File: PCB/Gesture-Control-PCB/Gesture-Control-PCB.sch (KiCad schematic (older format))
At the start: 5 parts, among them J1 Jack-DC, J2 Conn_01x07_Female, U1 L7806CV, U2 LD1117V33, U3 NodeMCU1.0(ESP-12E)

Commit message: decrease size, fit all components under nodemcu
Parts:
- U1, U2: footprint Package_TO_SOT_THT:TO-220-3_Vertical -> Package_TO_SOT_THT:TO-220-3_Horizontal_TabDown
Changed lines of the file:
@@
 F 0 "U2" H 3050 4092 50  0000 C CNN
 F 1 "LD1117V33" H 3050 4001 50  0000 C CNN
-F 2 "Package_TO_SOT_THT:TO-220-3_Vertical" H 3075 3700 50  0001 L CIN
+F 2 "Package_TO_SOT_THT:TO-220-3_Horizontal_TabDown" H 3075 3700 50  0001 L CIN
 F 3 "http://www.st.com/content/ccc/resource/technical/document/datasheet/41/4f/b3/b0/12/d4/47/88/CD00000444.pdf/files/CD00000444.pdf/jcr:content/translations/en.CD00000444.pdf" H 3050 3800 50  0001 C CNN
 	1    3050 3850
@@
 F 0 "U1" H 3050 3242 50  0000 C CNN
 F 1 "L7806CV" H 3050 3151 50  0000 C CNN
-F 2 "Package_TO_SOT_THT:TO-220-3_Vertical" H 3075 2850 50  0001 L CIN
+F 2 "Package_TO_SOT_THT:TO-220-3_Horizontal_TabDown" H 3075 2850 50  0001 L CIN
 F 3 "http://www.st.com/content/ccc/resource/technical/document/datasheet/41/4f/b3/b0/12/d4/47/88/CD00000444.pdf/files/CD00000444.pdf/jcr:content/translations/en.CD00000444.pdf" H 3050 2950 50  0001 C CNN
 	1    3050 3000

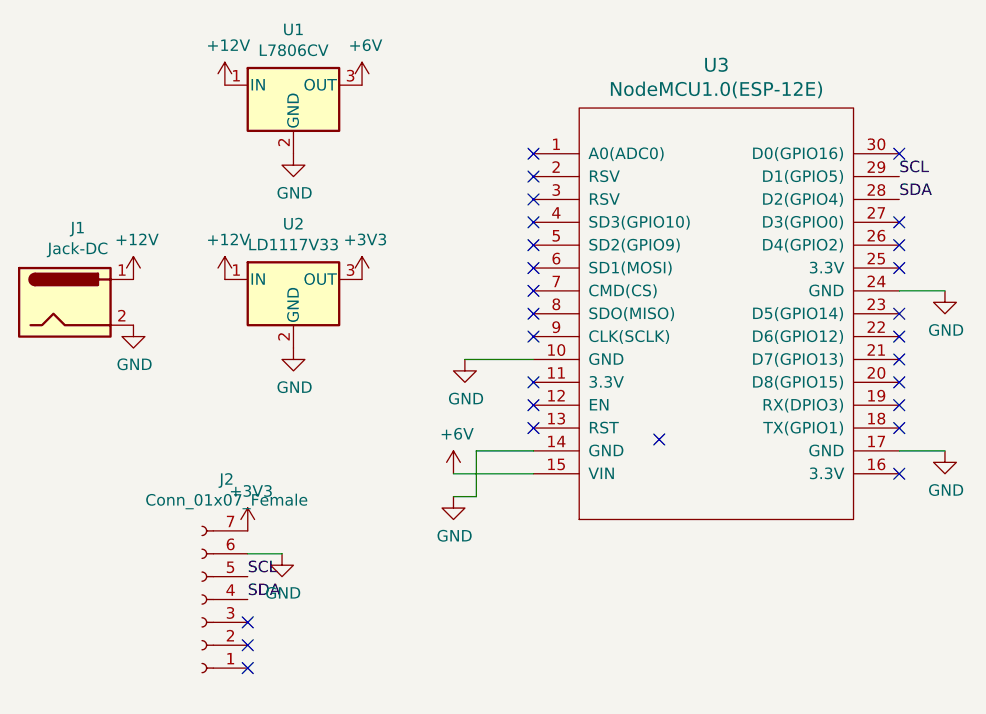
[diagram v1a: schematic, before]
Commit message: removed one voltage regulator (lmao im a dummy)
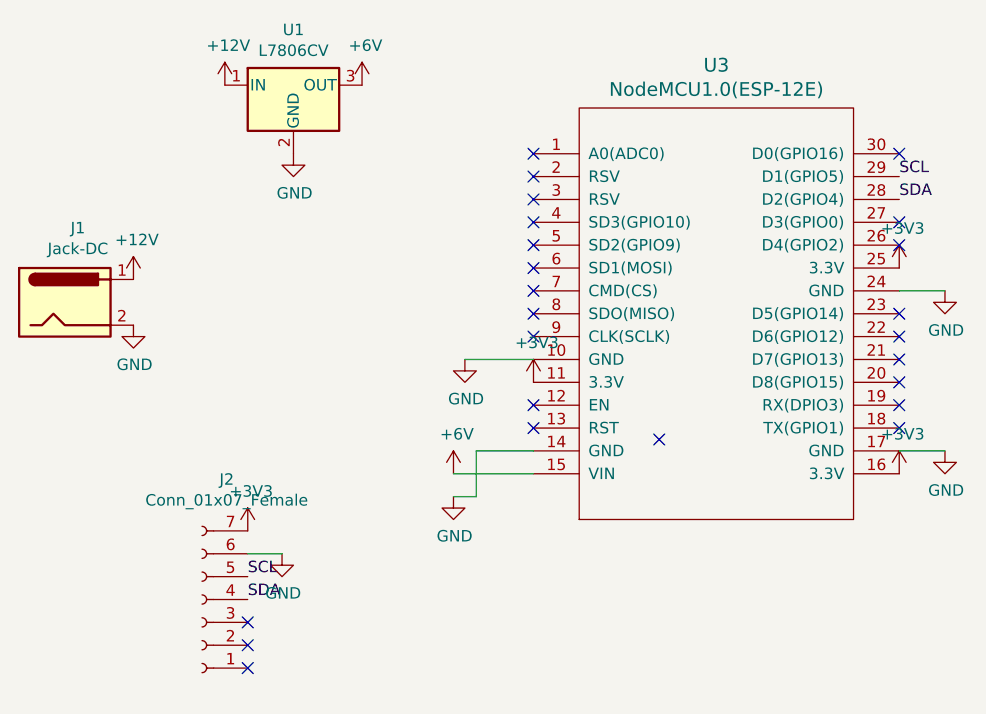
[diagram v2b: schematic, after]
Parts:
- removed U2: LD1117V33, Package_TO_SOT_THT:TO-220-3_Horizontal_TabDown, symbol Regulator_Linear:L7805
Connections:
- net +3V3: now also U3.11 (3.3V), U3.16 (3.3V), U3.25 (3.3V)
- no-connect marks 27 -> 24
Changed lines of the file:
@@
-$EndComp
-$Comp
-L Regulator_Linear:L7805 U2
-U 1 1 5FB5574C
-P 3050 3850
-F 0 "U2" H 3050 4092 50  0000 C CNN
-F 1 "LD1117V33" H 3050 4001 50  0000 C CNN
-F 2 "Package_TO_SOT_THT:TO-220-3_Horizontal_TabDown" H 3075 3700 50  0001 L CIN
-F 3 "http://www.st.com/content/ccc/resource/technical/document/datasheet/41/4f/b3/b0/12/d4/47/88/CD00000444.pdf/files/CD00000444.pdf/jcr:content/translations/en.CD00000444.pdf" H 3050 3800 50  0001 C CNN
-	1    3050 3850
-	1    0    0    -1
-$EndComp
-$Comp
-L power:+12V #PWR04
-U 1 1 5FB56752
-P 2750 3850
-F 0 "#PWR04" H 2750 3700 50  0001 C CNN
-F 1 "+12V" H 2765 4023 50  0000 C CNN
-F 2 "" H 2750 3850 50  0001 C CNN
-F 3 "" H 2750 3850 50  0001 C CNN
-	1    2750 3850
-	1    0    0    -1
-$EndComp
-$Comp
-L power:GND #PWR08
-U 1 1 5FB56B3F
-P 3050 4150
-F 0 "#PWR08" H 3050 3900 50  0001 C CNN
-F 1 "GND" H 3055 3977 50  0000 C CNN
-F 2 "" H 3050 4150 50  0001 C CNN
-F 3 "" H 3050 4150 50  0001 C CNN
-	1    3050 4150
-	1    0    0    -1
-$EndComp
-$Comp
-L power:+3V3 #PWR010
-U 1 1 5FB57184
-P 3350 3850
-F 0 "#PWR010" H 3350 3700 50  0001 C CNN
-F 1 "+3V3" H 3365 4023 50  0000 C CNN
-F 2 "" H 3350 3850 50  0001 C CNN
-F 3 "" H 3350 3850 50  0001 C CNN
-	1    3350 3850
-	1    0    0    -1
 $EndComp
 $Comp
@@
 NoConn ~ 4100 4000
 NoConn ~ 4100 4100
-NoConn ~ 4100 4300
 NoConn ~ 4100 4400
 NoConn ~ 4100 4500
-NoConn ~ 5700 4700
 NoConn ~ 5700 4500
 NoConn ~ 5700 4400
@@
 NoConn ~ 5700 4100
 NoConn ~ 5700 4000
-NoConn ~ 5700 3800
 NoConn ~ 5700 3700
 NoConn ~ 5700 3600
@@
 NoConn ~ 5700 3300
 NoConn ~ 4650 4550
+$Comp
+L power:+3V3 #PWR08
+U 1 1 5FB5C1C7
+P 5700 3800
+F 0 "#PWR08" H 5700 3650 50  0001 C CNN
+F 1 "+3V3" H 5715 3973 50  0000 C CNN
+F 2 "" H 5700 3800 50  0001 C CNN
+F 3 "" H 5700 3800 50  0001 C CNN
+	1    5700 3800
+	1    0    0    -1
+$EndComp
+$Comp
+L power:+3V3 #PWR010
+U 1 1 5FB5E0A4
+P 5700 4700
+F 0 "#PWR010" H 5700 4550 50  0001 C CNN
+F 1 "+3V3" H 5715 4873 50  0000 C CNN
+F 2 "" H 5700 4700 50  0001 C CNN
+F 3 "" H 5700 4700 50  0001 C CNN
+	1    5700 4700
+	1    0    0    -1
+$EndComp
+$Comp
+L power:+3V3 #PWR04
+U 1 1 5FB5EB1B
+P 4100 4300
+F 0 "#PWR04" H 4100 4150 50  0001 C CNN
+F 1 "+3V3" H 4115 4473 50  0000 C CNN
+F 2 "" H 4100 4300 50  0001 C CNN
+F 3 "" H 4100 4300 50  0001 C CNN
+	1    4100 4300
+	1    0    0    -1
+$EndComp
 $EndSCHEMATC

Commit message: fixed mpu socket and moved shit to bottom layer
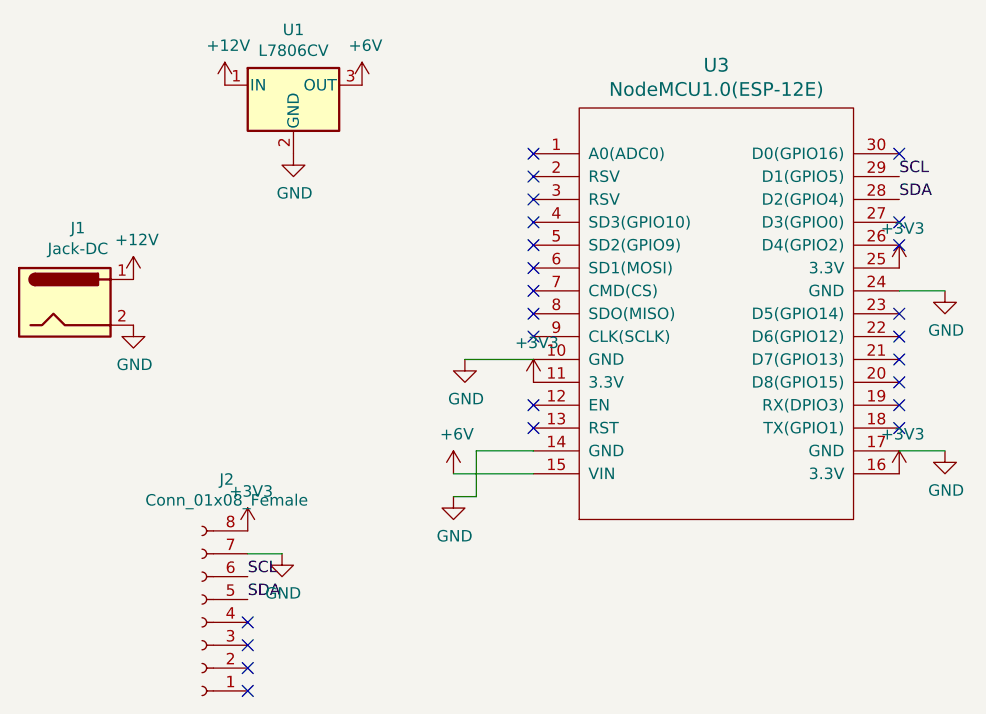
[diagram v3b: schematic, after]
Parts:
- removed J2: Conn_01x07_Female, Connector_PinSocket_2.00mm:PinSocket_1x07_P2.00mm_Vertical, symbol Connector:Conn_01x07_Female
- added J2: Conn_01x08_Female, Connector_PinSocket_2.54mm:PinSocket_1x08_P2.54mm_Vertical, symbol Connector:Conn_01x08_Female
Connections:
- net +3V3: now also J2.8 (Pin_8)
- net GND: now also J2.7 (Pin_7)
- net SCL: now also J2.6 (Pin_6)
- net SDA: now also J2.5 (Pin_5)
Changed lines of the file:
@@
 Text Label 2850 5150 0    50   ~ 0
 SCL
-$Comp
-L Connector:Conn_01x07_Female J2
-U 1 1 5FB66EDE
-P 2650 5250
-F 0 "J2" H 2542 4725 50  0000 C CNN
-F 1 "Conn_01x07_Female" H 2542 4816 50  0000 C CNN
-F 2 "Connector_PinSocket_2.00mm:PinSocket_1x07_P2.00mm_Vertical" H 2650 5250 50  0001 C CNN
-F 3 "~" H 2650 5250 50  0001 C CNN
-	1    2650 5250
-	-1   0    0    1
-$EndComp
 Text Label 5700 3400 0    50   ~ 0
 SCL
@@
 Text Label 5700 3500 0    50   ~ 0
 SDA
-NoConn ~ 2850 5350
-NoConn ~ 2850 5450
-NoConn ~ 2850 5550
 NoConn ~ 4100 3300
 NoConn ~ 4100 3400
@@
 	3800 4200 4100 4200
 NoConn ~ 5700 3300
-NoConn ~ 4650 4550
 $Comp
 L power:+3V3 #PWR08
@@
 	1    0    0    -1
 $EndComp
+$Comp
+L Connector:Conn_01x08_Female J2
+U 1 1 5FB6B29C
+P 2650 5350
+F 0 "J2" H 2542 4725 50  0000 C CNN
+F 1 "Conn_01x08_Female" H 2542 4816 50  0000 C CNN
+F 2 "Connector_PinSocket_2.54mm:PinSocket_1x08_P2.54mm_Vertical" H 2650 5350 50  0001 C CNN
+F 3 "~" H 2650 5350 50  0001 C CNN
+	1    2650 5350
+	-1   0    0    1
+$EndComp
+NoConn ~ 2850 5350
+NoConn ~ 2850 5450
+NoConn ~ 2850 5550
+NoConn ~ 2850 5650
 $EndSCHEMATC
